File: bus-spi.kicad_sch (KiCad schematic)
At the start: 3 parts

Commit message: Fixing lots of ERC errors
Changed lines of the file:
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@@
 		(comment 3 "Flight Club, W6YX, Endurance")
-	)
-	(junction
-		(at 133.35 88.9)
-		(diameter 0)
-		(color 0 0 0 0)
-	)
-	(junction
-		(at 133.35 96.52)
-		(diameter 0)
-		(color 0 0 0 0)
-	)
-	(junction
-		(at 133.35 81.28)
-		(diameter 0)
-		(color 0 0 0 0)
 	)
 	(bus_entry
@@
 		)
 	)
-	(wire
-		(pts
-			(xy 127 81.28) (xy 133.35 81.28)
-		)
-		(stroke
-			(width 0)
-			(type default)
-		)
-	)
 	(bus
 		(pts
@@
 		(pts
 			(xy 157.48 99.06) (xy 154.94 99.06)
-		)
-		(stroke
-			(width 0)
-			(type default)
-		)
-	)
-	(wire
-		(pts
-			(xy 127 96.52) (xy 133.35 96.52)
 		)
 		(stroke
@@
 	(wire
 		(pts
-			(xy 127 88.9) (xy 133.35 88.9)
-		)
-		(stroke
-			(width 0)
-			(type default)
-		)
-	)
-	(wire
-		(pts
 			(xy 133.35 81.28) (xy 152.4 81.28)
 		)
@@
 	)
 	(label "SPI.MISO"
-		(at 127 96.52 180)
+		(at 133.35 96.52 180)
 		(fields_autoplaced yes)
 		(effects
@@
 	)
 	(label "SPI.MOSI"
-		(at 127 88.9 180)
+		(at 133.35 88.9 180)
 		(fields_autoplaced yes)
 		(effects
@@
 	)
 	(label "SPI.SCK"
-		(at 127 81.28 180)
+		(at 133.35 81.28 180)
 		(fields_autoplaced yes)
 		(effects

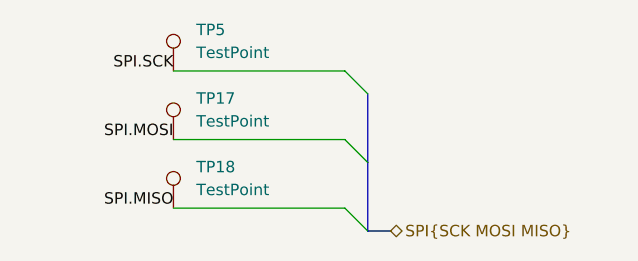
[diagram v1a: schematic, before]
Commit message: Redid board layout. Still have to add bypass caps
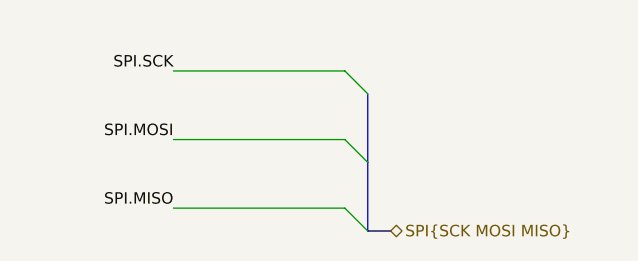
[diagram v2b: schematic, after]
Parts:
- removed TP17, TP18, TP5: TestPoint, TestPoint:TestPoint_Loop_D2.50mm_Drill1.0mm, symbol Connector:TestPoint
